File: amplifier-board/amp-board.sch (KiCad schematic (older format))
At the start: 32 parts, among them K1 CONN_3, P1 CONN_7, P2 CONN_7, U1 AD8618, U3 INA128, U4 ad7694

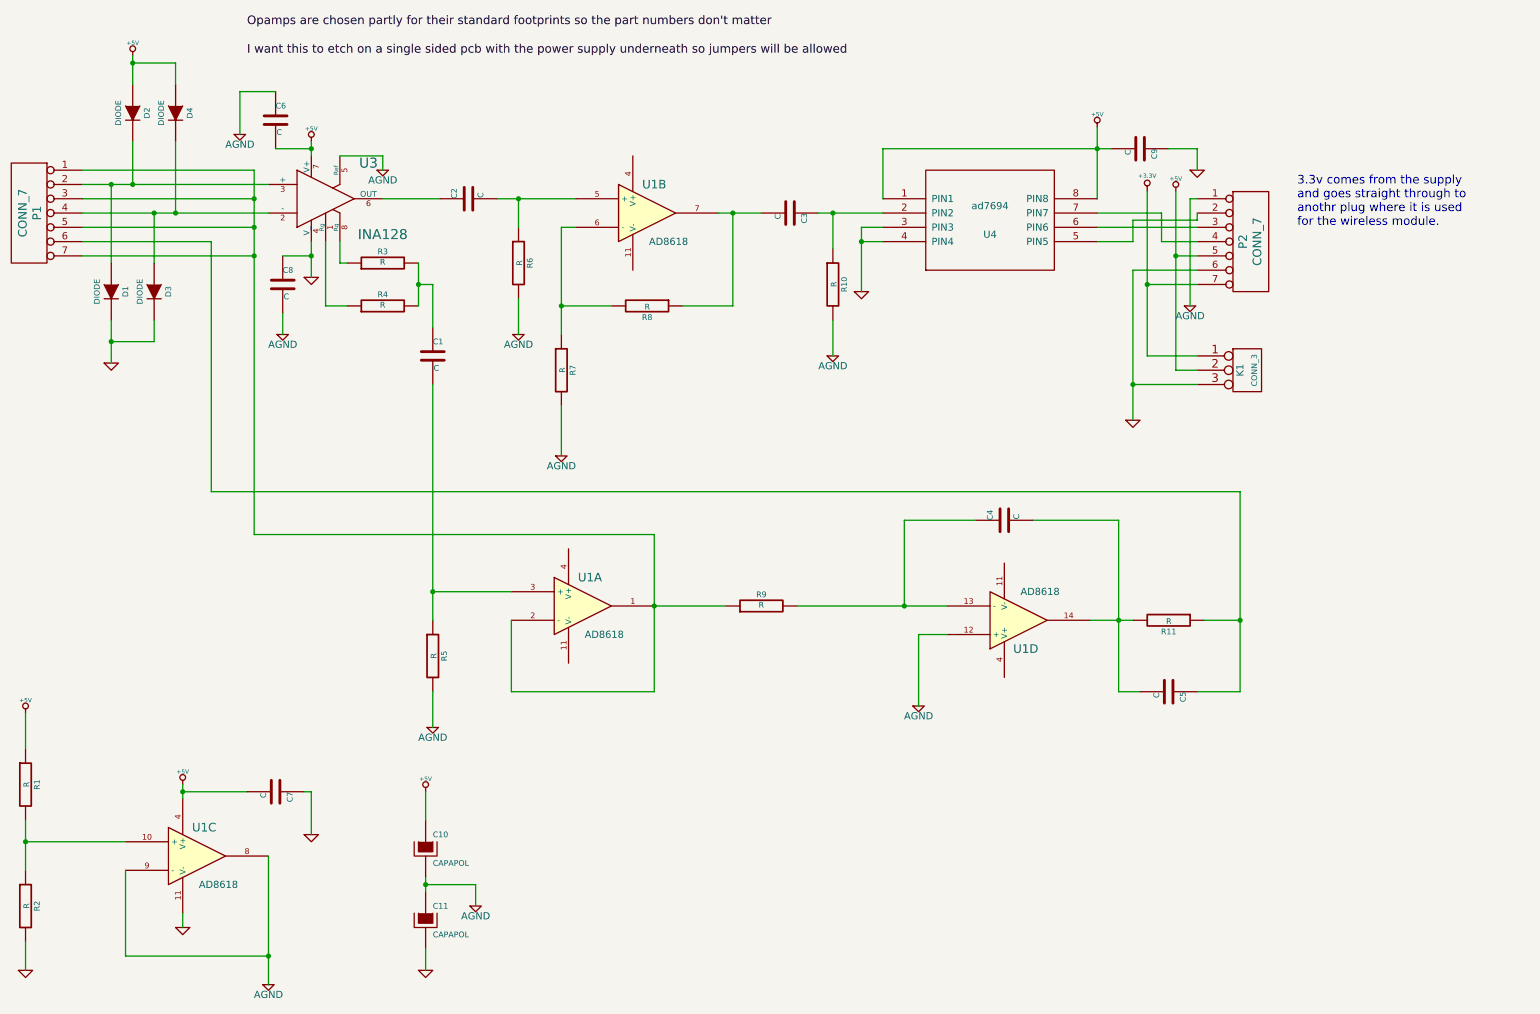
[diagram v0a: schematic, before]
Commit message: fixed diodes on amplifier pcb
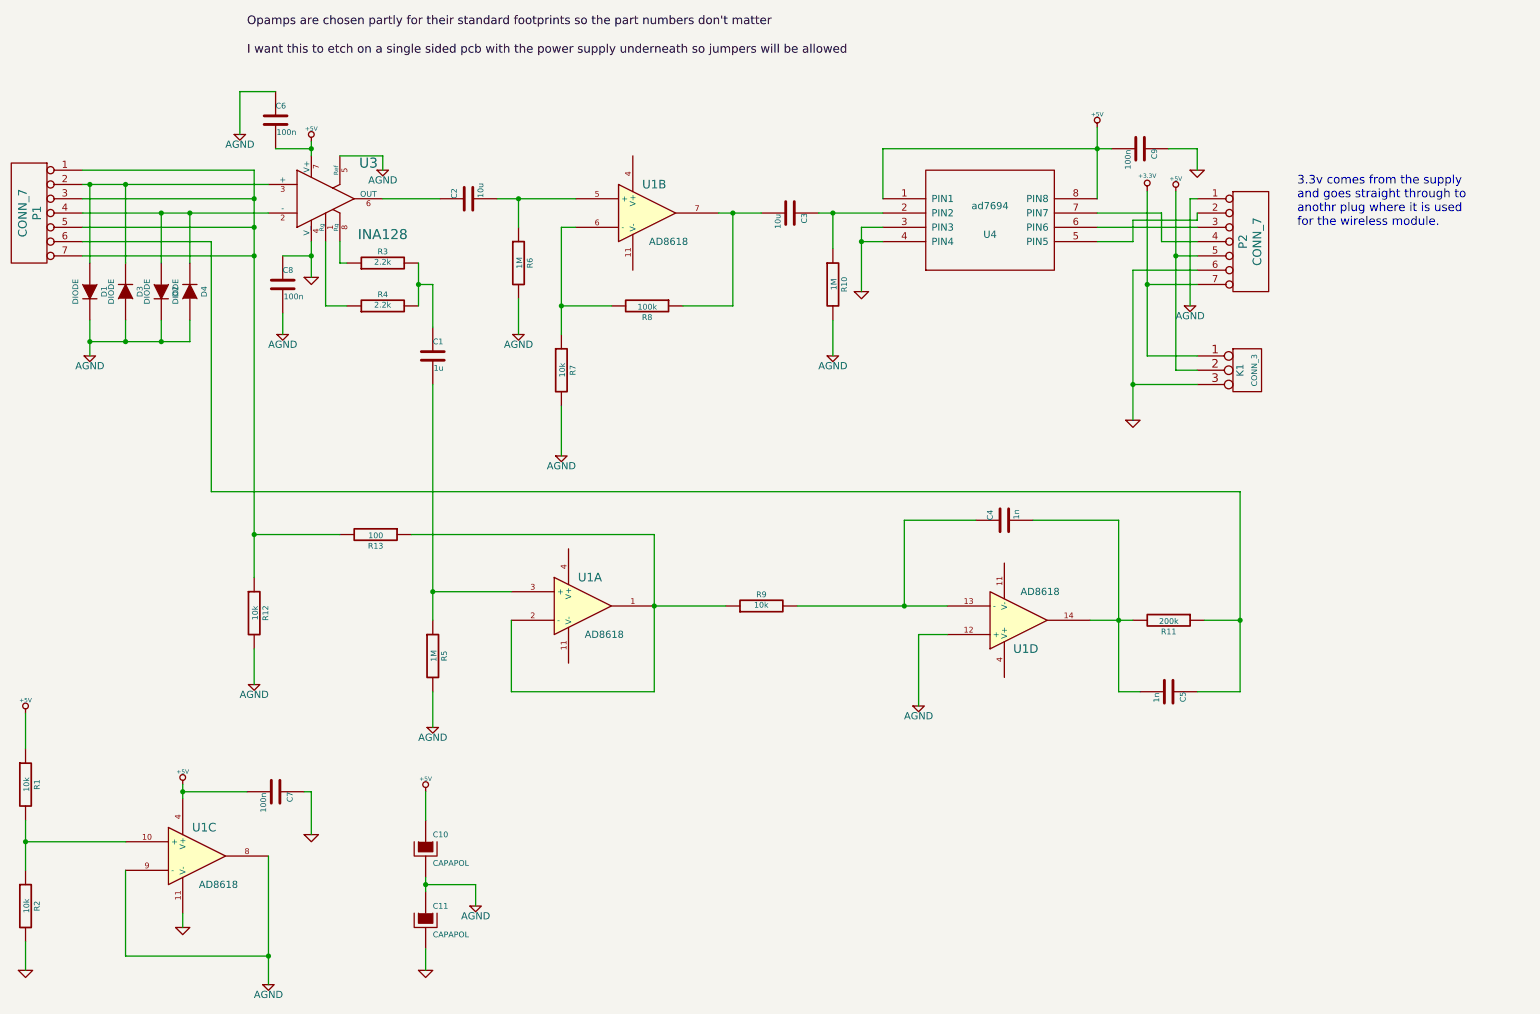
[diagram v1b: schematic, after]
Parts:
- added R12: 10k, ~, symbol R
- added R13: 100, ~, symbol R
- C1: value C -> 1u
- C2, C3: value C -> 10u
- C4, C5: value C -> 1n
- C6, C7, C8, C9: value C -> 100n
- R1, R2, R7, R9: value R -> 10k
- R10, R5, R6: value R -> 1M
- R11: value R -> 200k
- R3, R4: value R -> 2.2k
- R8: value R -> 100k
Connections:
- net +5V: no longer D2.1 (A), D4.1 (A)
- net AGND: now also D1.2 (K), D2.2 (K), D3.1 (A), D4.1 (A), R12.2
- net GND: no longer D1.2 (K), D3.2 (K)
- net at D4.2 (K), P1.4 (P4), U3.2 (-): now also D2.1 (A); no longer D3.1 (A)
- net at D1.1 (A), P1.2 (P2), U3.3 (+): now also D3.2 (K); no longer D2.2 (K)
- net at P1.1 (P1), P1.3 (P3), P1.5 (P5)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: now also R12.1, R13.2; no longer R9.1, U1.1, U1.2 (-)
- new net: R13.1, R9.1, U1.1, U1.2 (-)
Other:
- moved on the sheet: D1, D2, D3, D4

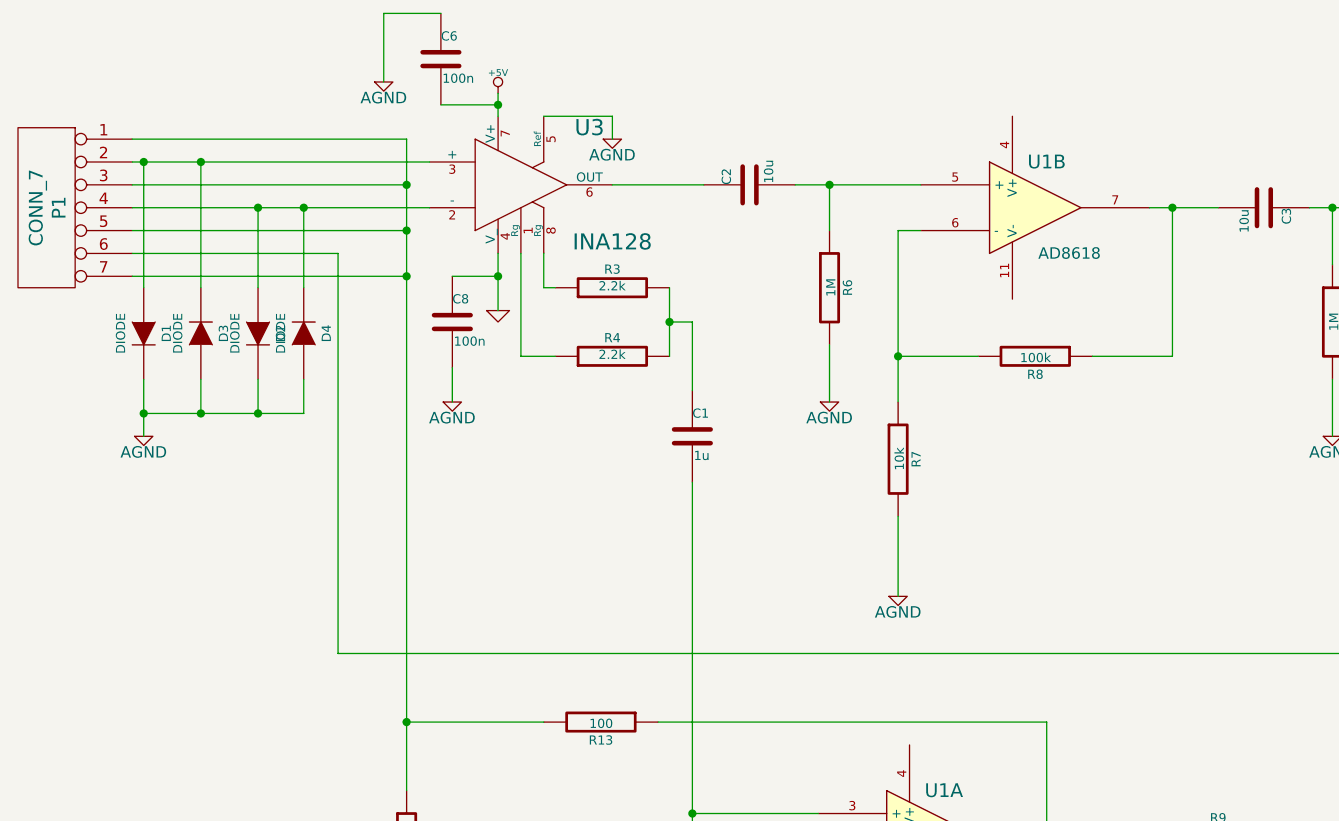
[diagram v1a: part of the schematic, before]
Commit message: added discontinued notice
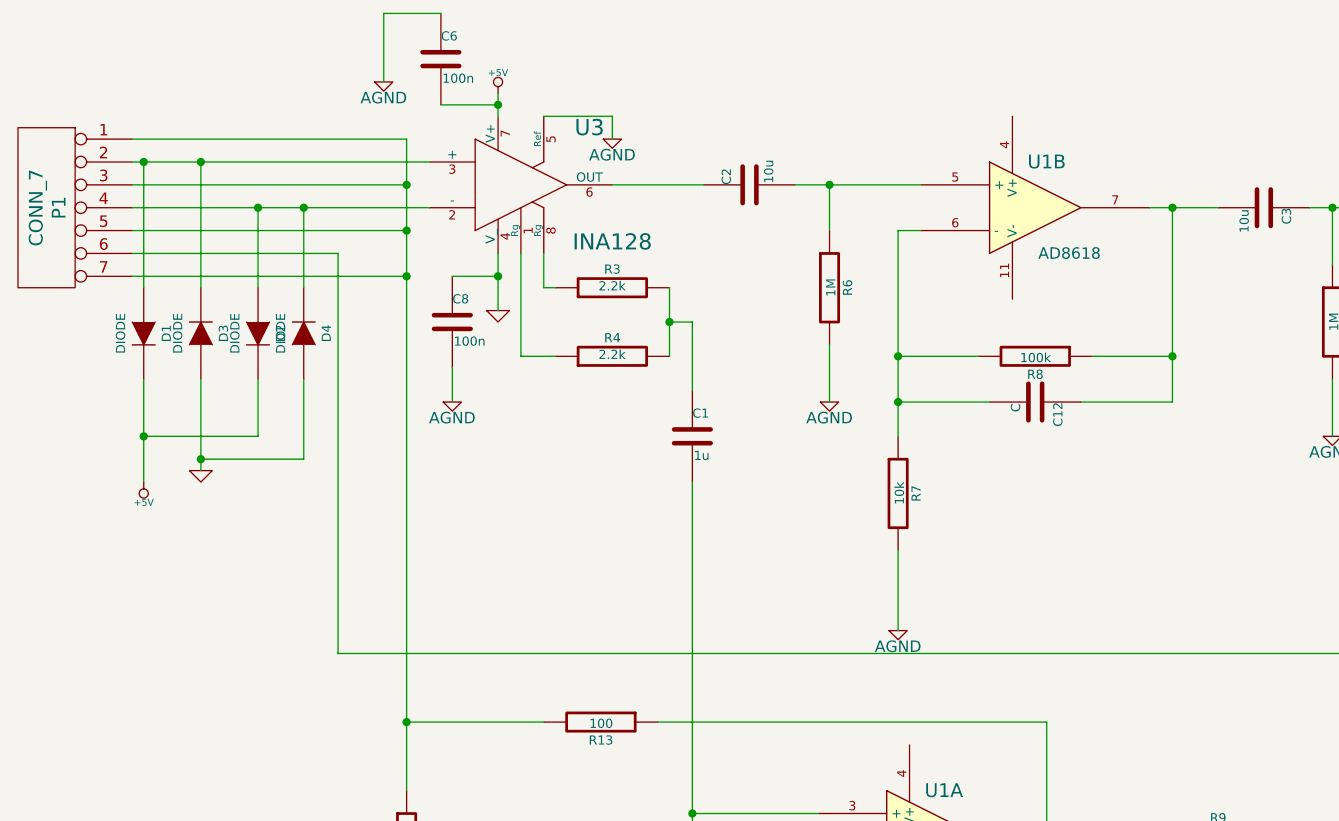
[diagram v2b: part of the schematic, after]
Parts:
- added C12: C, ~, symbol C
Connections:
- net +5V: now also D1.2 (K), D2.2 (K)
- net AGND: no longer D1.2 (K), D2.2 (K), D3.1 (A), D4.1 (A)
- net GND: now also D3.1 (A), D4.1 (A)
- net at R7.1, R8.2, U1.6 (-): now also C12.2
- net at C3.2, R8.1, U1.7: now also C12.1
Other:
- moved on the sheet: R7
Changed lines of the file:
@@
 Sheet 1 1
 Title ""
-Date "15 feb 2016"
+Date "1 apr 2016"
 Rev ""
 Comp ""
@@
 L R R7
 U 1 1 569FB13E
-P 4700 3000
-F 0 "R7" V 4780 3000 40  0000 C CNN
-F 1 "10k" V 4707 3001 40  0000 C CNN
-F 2 "~" V 4630 3000 30  0000 C CNN
-F 3 "~" H 4700 3000 30  0000 C CNN
-	1    4700 3000
+P 4700 3150
+F 0 "R7" V 4780 3150 40  0000 C CNN
+F 1 "10k" V 4707 3151 40  0000 C CNN
+F 2 "~" V 4630 3150 30  0000 C CNN
+F 3 "~" H 4700 3150 30  0000 C CNN
+	1    4700 3150
 	1    0    0    -1
 $EndComp
@@
 L AGND #PWR09
 U 1 1 569FB157
-P 4700 3600
-F 0 "#PWR09" H 4700 3600 40  0001 C CNN
-F 1 "AGND" H 4700 3530 50  0000 C CNN
-F 2 "" H 4700 3600 60  0000 C CNN
-F 3 "" H 4700 3600 60  0000 C CNN
-	1    4700 3600
+P 4700 3750
+F 0 "#PWR09" H 4700 3750 40  0001 C CNN
+F 1 "AGND" H 4700 3680 50  0000 C CNN
+F 2 "" H 4700 3750 60  0000 C CNN
+F 3 "" H 4700 3750 60  0000 C CNN
+	1    4700 3750
 	1    0    0    -1
 $EndComp
@@
 $EndComp
 $Comp
-L AGND #PWR028
-U 1 1 56C14137
-P 1400 2900
-F 0 "#PWR028" H 1400 2900 40  0001 C CNN
-F 1 "AGND" H 1400 2830 50  0000 C CNN
-F 2 "" H 1400 2900 60  0000 C CNN
-F 3 "" H 1400 2900 60  0000 C CNN
-	1    1400 2900
+L C C12
+U 1 1 56C27B5C
+P 5300 2750
+F 0 "C12" H 5300 2850 40  0000 L CNN
+F 1 "C" H 5306 2665 40  0000 L CNN
+F 2 "~" H 5338 2600 30  0000 C CNN
+F 3 "~" H 5300 2750 60  0000 C CNN
+	1    5300 2750
+	0    1    1    0
+$EndComp
+$Comp
+L GND #PWR?
+U 1 1 56FF0129
+P 1650 3050
+F 0 "#PWR?" H 1650 3050 30  0001 C CNN
+F 1 "GND" H 1650 2980 30  0001 C CNN
+F 2 "" H 1650 3050 60  0000 C CNN
+F 3 "" H 1650 3050 60  0000 C CNN
+	1    1650 3050
 	1    0    0    -1
 $EndComp
@@
 	7200 4850 7400 4850
 Wire Wire Line
-	4700 2000 4700 2750
+	4700 2000 4700 2900
 Wire Wire Line
 	4700 2000 4800 2000
@@
 	5550 2550 5900 2550
 Wire Wire Line
-	5900 2550 5900 1900
+	5900 1900 5900 2750
 Connection ~ 5900 1900
 Wire Wire Line
-	4700 3250 4700 3600
+	4700 3400 4700 3750
 Wire Wire Line
 	6500 1900 6950 1900
@@
 	5350 4150 3650 4150
 Wire Wire Line
-	1400 2900 1400 2650
-Wire Wire Line
-	2100 2650 2100 2800
-Wire Wire Line
-	2100 2800 1400 2800
-Connection ~ 1400 2800
-Wire Wire Line
 	1350 1900 2650 1900
 Wire Wire Line
-	2650 1700 1350 1700
-Wire Wire Line
-	1650 2650 1650 2800
-Connection ~ 1650 2800
-Wire Wire Line
-	1900 2650 1900 2800
-Connection ~ 1900 2800
+	1350 1700 2650 1700
 Wire Wire Line
 	2100 2250 2100 1900
@@
 	1400 2250 1400 1700
 Connection ~ 1400 1700
+Wire Wire Line
+	5100 2750 4700 2750
+Connection ~ 4700 2750
+Wire Wire Line
+	5900 2750 5500 2750
+Connection ~ 5900 2550
+Wire Wire Line
+	1650 2650 1650 3050
+Connection ~ 1650 3000
+$Comp
+L +5V #PWR?
+U 1 1 56FF0451
+P 1400 3100
+F 0 "#PWR?" H 1400 3190 20  0001 C CNN
+F 1 "+5V" H 1400 3190 30  0000 C CNN
+F 2 "" H 1400 3100 60  0000 C CNN
+F 3 "" H 1400 3100 60  0000 C CNN
+	1    1400 3100
+	1    0    0    1
+$EndComp
+Wire Wire Line
+	1400 3100 1400 2650
+Connection ~ 1400 2900
+Wire Wire Line
+	1650 3000 2100 3000
+Wire Wire Line
+	2100 3000 2100 2650
+Wire Wire Line
+	1400 2900 1900 2900
+Wire Wire Line
+	1900 2900 1900 2650
 $EndSCHEMATC
